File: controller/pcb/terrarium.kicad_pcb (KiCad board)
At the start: 2 copper layers, 90 x 90 mm, 46 parts, among them Q1 S8050, Q2 S8050, Q3 S8050, U1 DS3231M

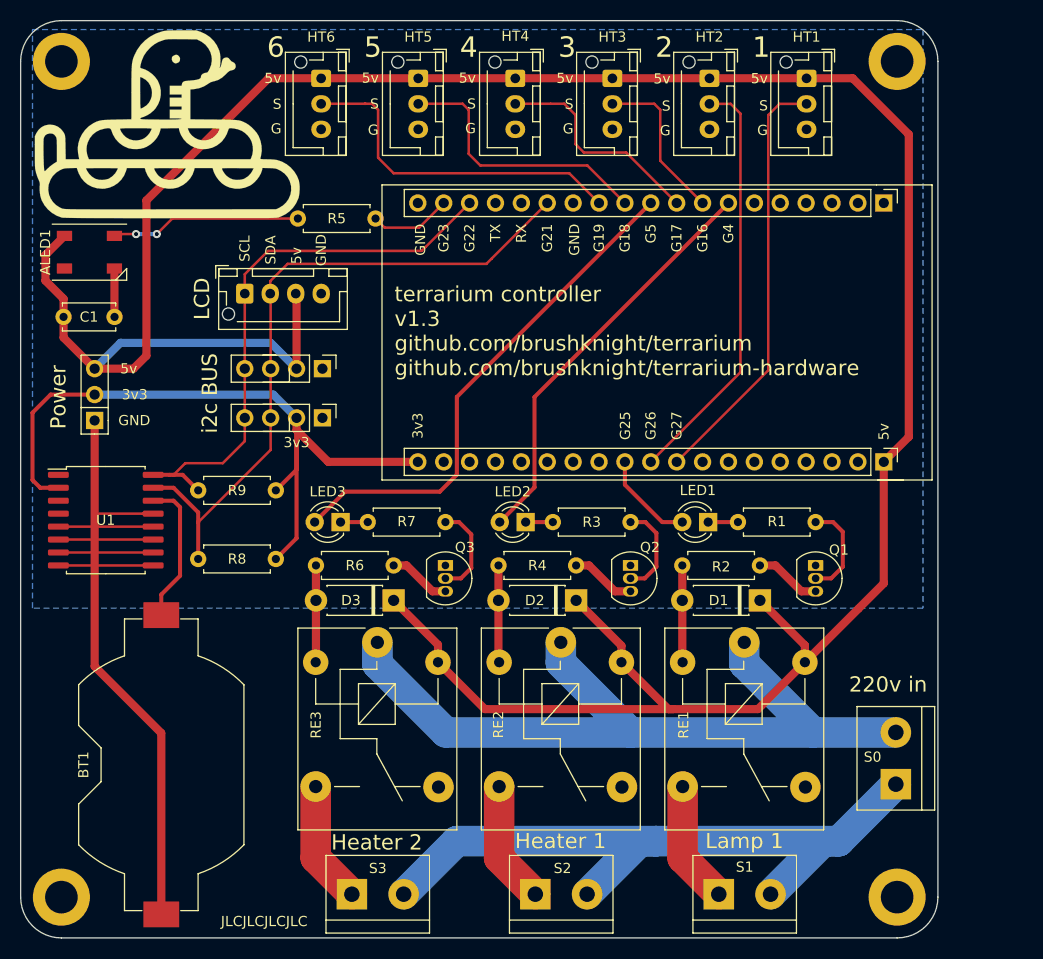
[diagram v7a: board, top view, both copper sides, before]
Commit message: pcb: add esp32
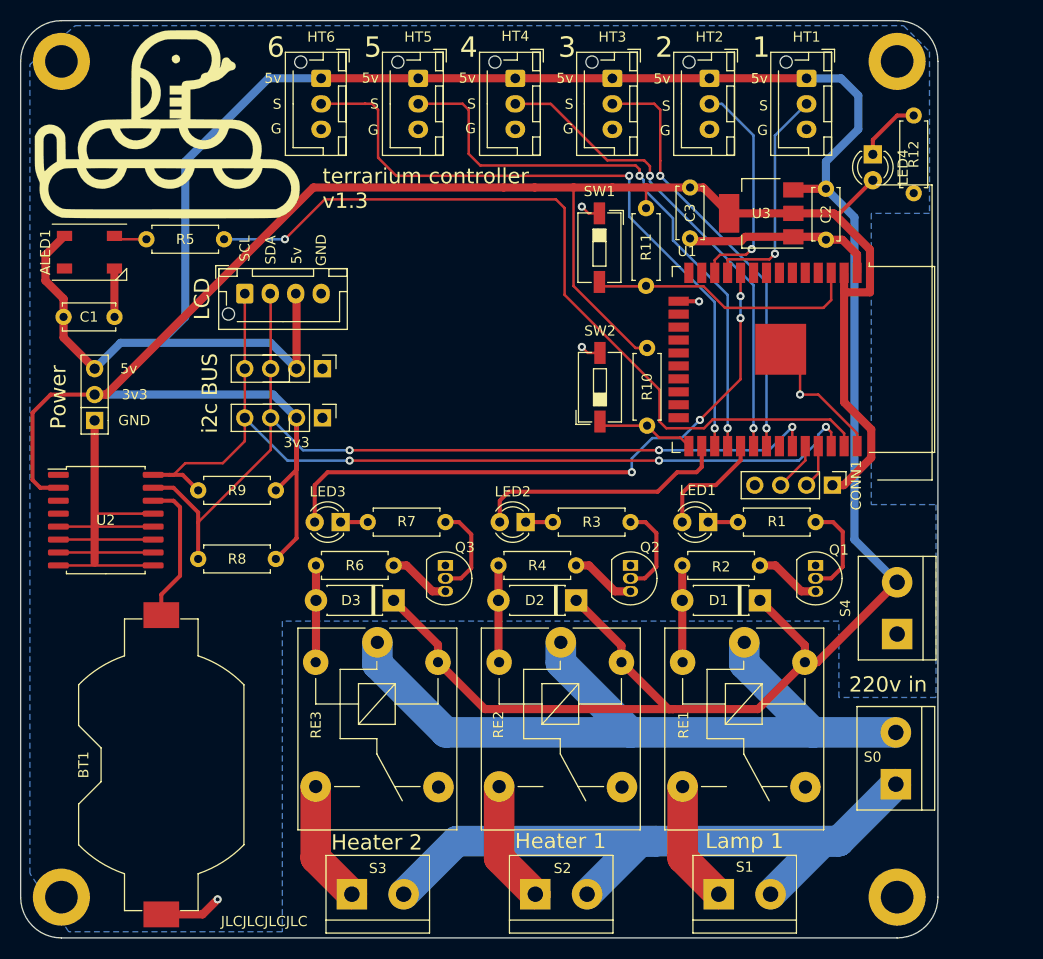
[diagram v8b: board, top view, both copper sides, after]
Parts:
- removed esp32-left1, esp32-right1: Conn_01x19_MountingPin, Connector_PinHeader_2.54mm:PinHeader_1x19_P2.54mm_Vertical
- added C2: 10uF, Capacitor_THT:C_Disc_D5.0mm_W2.5mm_P5.00mm, F.Cu at (120.0, 39.5)
- added C3: 47uF, Capacitor_THT:C_Disc_D5.0mm_W2.5mm_P5.00mm, F.Cu at (106.7, 39.4)
- added CONN1: data, Connector_PinHeader_2.54mm:PinHeader_1x04_P2.54mm_Vertical, F.Cu at (120.7, 68.6)
- added LED4: POWER, LED_THT:LED_D3.0mm_Clear, F.Cu at (124.6, 36.1)
- added R10: 10k, Resistor_THT:R_Axial_DIN0207_L6.3mm_D2.5mm_P7.62mm_Horizontal, F.Cu at (102.5, 55.1)
- added R11: 10k, Resistor_THT:R_Axial_DIN0207_L6.3mm_D2.5mm_P7.62mm_Horizontal, F.Cu at (102.4, 41.4)
- added R12: 300, Resistor_THT:R_Axial_DIN0207_L6.3mm_D2.5mm_P7.62mm_Horizontal, F.Cu at (128.6, 39.9)
- added S4: 5v in, TerminalBlock:TerminalBlock_bornier-2_P5.08mm, F.Cu at (127.0, 83.2)
- added SW1: SW_Push, Button_Switch_SMD:SW_DIP_SPSTx01_Slide_6.7x4.1mm_W6.73mm_P2.54mm_LowProfile_JPin, F.Cu at (97.8, 45.3)
- added SW2: SW_Push, Button_Switch_SMD:SW_DIP_SPSTx01_Slide_6.7x4.1mm_W6.73mm_P2.54mm_LowProfile_JPin, F.Cu at (97.8, 59.0)
- added U1: ESP32-WROOM-32, RF_Module:ESP32-WROOM-32, F.Cu at (114.8, 56.2)
- added U3: LM1117-3.3, Package_TO_SOT_SMD:SOT-223-3_TabPin2, F.Cu at (113.7, 41.9)
- moved R5 15.0 mm to (61.0, 44.5)
- renumbered U1 to U2
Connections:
- HT1 pad 2: G27 -> G26
- HT2 pad 2: G26 -> G27
- HT3 pad 2: G16 -> G19
- HT4 pad 2: G17 -> G18
- HT5 pad 2: G18 -> G17
- HT6 pad 2: G19 -> G16
- LED1 pad 2: G25 -> G5
- LED3 pad 2: G5 -> G25
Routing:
- net +3V3: track 74.1 -> 204.8 mm
- net G23: track 8.06 -> 80.7 mm, vias 0 -> 1
- net G25: track 9.39 -> 60.9 mm, vias 0 -> 4
- net G16: track 16.2 -> 66.0 mm, vias 0 -> 2
- net G5: track 50.4 -> 11.3 mm
- net G17: track 21.5 -> 57.6 mm, vias 0 -> 2
- net SCL: track 55.0 -> 90.7 mm, vias 0 -> 3
- net Net-(R11-Pad2): track 0.00 -> 26.8 mm
- net SDA: track 67.2 -> 91.0 mm, vias 0 -> 3
- net G18: track 26.8 -> 47.4 mm, vias 0 -> 2
- net G27: track 42.0 -> 23.6 mm, vias 0 -> 1
- net G26: track 41.3 -> 23.1 mm, vias 0 -> 1
- net G4: track 41.0 -> 25.7 mm
- net Net-(ALED1-Pad4): track 18.7 -> 3.53 mm, vias 2 -> 0
- net GND: track 117.5 -> 107.4 mm, vias 0 -> 5
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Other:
- board text added: "terrarium controller v1.3"
- board text removed: "G16"
- board text removed: "G17"
- board text removed: "G18"
- board text removed: "G19"
- board text removed: "G21"
- board text removed: "G22"
- board text removed: "G23"
- board text removed: "G25"
- board text removed: "G26"
- board text removed: "G27"
- board text removed: "G4"
- board text removed: "G5"
- board text removed: "RX"
- board text removed: "TX"
